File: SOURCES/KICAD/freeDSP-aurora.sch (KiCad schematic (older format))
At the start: 76 parts, among them IC101 IC_ADAU1452, IC102 IC_25AA1024, IC103 IC_TLE2426ID, IC104 IC_ADM811TARTZ, IC105 IC_LM1117MP-5.0, IC106 IC_NCP1117LPST33, IC107 IC_LM1117MP-5.0, IC108 IC_LM1117MPX-ADJ, Q101 Q_STD2805, X101 MicroMatch14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

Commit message: Updated BOM
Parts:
- C101: Manufacturer (none) -> Murata Electronics North America; manf_num (none) -> GRM21BR61E106MA73L; pn (none) -> GRM21BR61E106MA73L
- C102, C105, C109, C110, C113, C118, C121, C124, C128, C129, C130, C131, C133, C134, C135, C136: Manufacturer (none) -> KEMET; pn (none) -> C0805C104K5RACTU
- C103: Manufacturer (none) -> Yageo; pn (none) -> CC0805KRX7R9BB562
- C104, C111, C112, C114, C117, C119, C120, C122, C123, C125, C127, C132, C137: Manufacturer (none) -> Murata Electronics North America; pn (none) -> GRM21BR61E106MA73L
- C106: Manufacturer (none) -> KEMET; pn (none) -> C0805C151J5GACTU
- C107, C108: Manufacturer (none) -> KEMET; pn (none) -> C0805C220J5GACTU
- C115, C116, C126: Manufacturer (none) -> Wurth Electronics Inc.; pn (none) -> 860010474012
- FER101, FER102: Manufacturer (none) -> Murata Electronics North America; pn (none) -> BLM21AG601SN1D
- IC101: Manufacturer (none) -> Analog Devices Inc.; pn (none) -> ADAU1452WBCPZ
- IC102: Manufacturer (none) -> Microchip Technology; pn (none) -> 25AA1024T-I/SM
- IC103: Manufacturer (none) -> Texas Instruments; pn (none) -> TLE2426IDR
- IC104: Manufacturer (none) -> Analog Devices Inc.; pn (none) -> ADM811TARTZ-REEL
- IC105, IC107: Manufacturer (none) -> Texas Instruments; pn (none) -> LM1117MP-5.0/NOPB
- IC106: Manufacturer (none) -> ON Semiconductor; pn (none) -> NCP1117LPST33T3G
- IC108: Manufacturer (none) -> Texas Instruments; pn (none) -> LM1117MPX-ADJ/NOPB
- JP101: Manufacturer (none) -> Wurth Electronics Inc.; pn (none) -> 61300211121
- Q101: Manufacturer (none) -> STMicroelectronics; pn (none) -> STD2805T4
- R101, R102, R104, R105: Manufacturer (none) -> Yageo; pn (none) -> TC164-JR-0733RL
- R103, R114: Manufacturer (none) -> Yageo; pn (none) -> RC0805FR-071KL
- R106: Manufacturer (none) -> Yageo; pn (none) -> RC0805FR-074K32L
- R107, R112, R113: Manufacturer (none) -> Yageo; pn (none) -> RC0805FR-0710KL
- R108: Manufacturer (none) -> Yageo; pn (none) -> RC0805FR-07100RL
- R109: Manufacturer (none) -> Yageo; pn (none) -> RC0805FR-0733RL
- R110, R111: Manufacturer (none) -> Yageo; pn (none) -> RC0805FR-072KL
- R115: Manufacturer (none) -> Yageo; pn (none) -> RC0805FR-07100KL
- R116: Manufacturer (none) -> Stackpole Electronics Inc.; pn (none) -> RNCP0805FTD150R
- R117: Manufacturer (none) -> Yageo; pn (none) -> RC0805FR-07931RL
- X101: Manufacturer (none) -> TE Connectivity AMP Connectors; pn (none) -> 1-215079-4
- X102: Manufacturer (none) -> Sullins Connector Solutions; pn (none) -> PRPC008DAAN-RC
- X103: Manufacturer (none) -> Sullins Connector Solutions; pn (none) -> PRPC003SAAN-RC
- X104: Manufacturer (none) -> TE Connectivity AMP Connectors; pn (none) -> 1-215079-0
- X105: Manufacturer (none) -> Molex, LLC; pn (none) -> 0430450428
- Y101: Manufacturer (none) -> EPSON; pn (none) -> FA-238 24.5760MB-K3

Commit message: Improved ADC input stage
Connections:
- wire segments 363 -> 367
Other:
- moved on the sheet: C112, C113, C114, C115, C116, C137, R116

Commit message: Added extra LDO for ESP32
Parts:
- removed C112, C114, C137: CAP_10u0_25V_X5R_0805, rklib:C0805-X7R, symbol rk:CAP_10u0_25V_X5R_0805
- removed C113: CAP_100n_50V_X7R_0805, rklib:C0805-X7R, symbol rk:CAP_100n_50V_X7R_0805
- removed IC108: IC_LM1117MPX-ADJ, rklib:SOT223, symbol rk:IC_LM1117MPX-ADJ
- removed R116: RES_150R_1%_0.25W_Thin_0805, rklib:C0805-RES, symbol rk:RES_150R_1%_0.25W_Thin_0805
- removed R117: RES_931R_1%_0.125W_Thick_0805, rklib:C0805-RES, symbol rk:RES_931R_1%_0.125W_Thick_0805
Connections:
- net labels removed: +9VA
- wire segments 367 -> 347
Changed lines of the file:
@@
-$EndComp
-$Comp
-L freeDSP-aurora-rescue:GND #PWR011
-U 1 1 590AE9CB
-P 7100 12500
-F 0 "#PWR011" H 7100 12250 50  0001 C CNN
-F 1 "GND" H 7100 12350 39  0000 C CNN
-F 2 "" H 7100 12500 50  0000 C CNN
-F 3 "" H 7100 12500 50  0000 C CNN
-	1    7100 12500
-	1    0    0    -1
-$EndComp
-$Comp
-L freeDSP-aurora-rescue:GND #PWR012
-U 1 1 590AE9E1
-P 6900 12500
-F 0 "#PWR012" H 6900 12250 50  0001 C CNN
-F 1 "GND" H 6900 12350 39  0000 C CNN
-F 2 "" H 6900 12500 50  0000 C CNN
-F 3 "" H 6900 12500 50  0000 C CNN
-	1    6900 12500
-	1    0    0    -1
-$EndComp
-$Comp
-L freeDSP-aurora-rescue:GND #PWR013
-U 1 1 590AEA02
-P 5900 12500
-F 0 "#PWR013" H 5900 12250 50  0001 C CNN
-F 1 "GND" H 5900 12350 39  0000 C CNN
-F 2 "" H 5900 12500 50  0000 C CNN
-F 3 "" H 5900 12500 50  0000 C CNN
-	1    5900 12500
-	1    0    0    -1
-$EndComp
-$Comp
-L freeDSP-aurora-rescue:+12V #PWR014
-U 1 1 590AEA0B
-P 5900 12100
-F 0 "#PWR014" H 5900 11950 50  0001 C CNN
-F 1 "+12V" H 5900 12240 39  0000 C CNN
-F 2 "" H 5900 12100 50  0000 C CNN
-F 3 "" H 5900 12100 50  0000 C CNN
-	1    5900 12100
-	1    0    0    -1
 $EndComp
 $Comp
@@
 Text Label 5050 5550 2    39   ~ 0
 AUXADC5
-$Comp
-L freeDSP-aurora-rescue:GND #PWR059
-U 1 1 59F06A35
-P 6100 12850
-F 0 "#PWR059" H 6100 12600 50  0001 C CNN
-F 1 "GND" H 6100 12700 39  0000 C CNN
-F 2 "" H 6100 12850 50  0000 C CNN
-F 3 "" H 6100 12850 50  0000 C CNN
-	1    6100 12850
-	1    0    0    -1
-$EndComp
-$Comp
-L freeDSP-aurora-rescue:GND #PWR060
-U 1 1 59F06B0F
-P 6350 12850
-F 0 "#PWR060" H 6350 12600 50  0001 C CNN
-F 1 "GND" H 6350 12700 39  0000 C CNN
-F 2 "" H 6350 12850 50  0000 C CNN
-F 3 "" H 6350 12850 50  0000 C CNN
-	1    6350 12850
-	1    0    0    -1
-$EndComp
 Wire Wire Line
 	1450 10400 1500 10400
@@
 Connection ~ 2800 10300
 Connection ~ 3000 10300
-Wire Wire Line
-	6900 12150 6900 12200
-Wire Wire Line
-	7100 12100 7100 12150
-Connection ~ 6900 12150
-Connection ~ 5900 12150
-Connection ~ 7100 12150
-Wire Wire Line
-	5950 12150 5900 12150
 Wire Wire Line
 	6550 4000 6500 4000
@@
 Wire Wire Line
 	4800 5550 5050 5550
-Wire Wire Line
-	6350 12450 6350 12500
-Wire Wire Line
-	6100 12500 6350 12500
-Connection ~ 6350 12500
-Wire Wire Line
-	6750 12500 6700 12500
-Wire Wire Line
-	6100 12500 6100 12550
 $Sheet
 S 1200 2850 2250 1750
@@
 	1    0    0    -1
 $EndComp
-$Comp
-L freeDSP-aurora-rescue:+9VA #PWR072
-U 1 1 5B7A7F08
-P 7100 12100
-F 0 "#PWR072" H 7100 11975 50  0001 C CNN
-F 1 "+9VA" H 7100 12250 39  0000 C CNN
-F 2 "" H 7100 12100 50  0001 C CNN
-F 3 "" H 7100 12100 50  0001 C CNN
-	1    7100 12100
-	1    0    0    -1
-$EndComp
 Text Label 4050 6400 2    39   ~ 0
 xSDA
@@
 $EndComp
 Wire Wire Line
-	7350 12150 7350 12200
-Wire Wire Line
-	7600 12150 7600 12200
-Connection ~ 7350 12150
-Wire Wire Line
-	6750 12150 6900 12150
-Wire Wire Line
 	4600 10400 4600 10450
 Connection ~ 4350 10400
-Wire Wire Line
-	5900 12100 5900 12150
 $Comp
 L freeDSP-aurora-rescue:+12V #PWR076
@@
 	3000 10300 3000 10450
 Wire Wire Line
-	6900 12150 7100 12150
-Wire Wire Line
-	5900 12150 5900 12200
-Wire Wire Line
-	7100 12150 7100 12200
-Wire Wire Line
-	7100 12150 7350 12150
-Wire Wire Line
 	6500 5600 6500 6100
 Wire Wire Line
@@
 	6900 3600 6800 3600
 Wire Wire Line
-	6350 12500 6350 12550
-Wire Wire Line
-	6350 12500 6400 12500
-Wire Wire Line
 	11950 3200 11950 3250
 Wire Wire Line
@@
 Wire Wire Line
 	3250 10300 3250 10450
-Wire Wire Line
-	7350 12150 7600 12150
 Wire Wire Line
 	4350 10400 4600 10400
@@
 F 8 "BLM21AG601SN1D" H 0   0   50  0001 C CNN "pn"
 	1    5650 4400
-	0    1    1    0
-$EndComp
-$Comp
-L rk:CAP_100n_50V_X7R_0805 C113
-U 1 1 5C1D47A6
-P 6900 12350
-F 0 "C113" H 7100 12400 39  0000 R CNN
-F 1 "CAP_100n_50V_X7R_0805" H 6900 12200 39  0001 C CNN
-F 2 "rklib:C0805-X7R" H 6900 12150 39  0001 C CNN
-F 3 "" H 6950 12400 50  0001 C CNN
-F 4 "100n" H 7100 12450 39  0000 R CNN "Value1"
-F 5 "5% 50V X7R" H 6900 12100 39  0001 C CNN "Value2"
-F 6 "399-1170-1-ND" H 6900 12050 39  0001 C CNN "digikey"
-F 7 "KEMET" H 650 1850 50  0001 C CNN "Manufacturer"
-F 8 "C0805C104K5RACTU" H 650 1850 50  0001 C CNN "pn"
-	1    6900 12350
 	0    1    1    0
 $EndComp
@@
 $EndComp
 $Comp
-L rk:CAP_10u0_25V_X5R_0805 C112
-U 1 1 5C5046DC
-P 5900 12350
-F 0 "C112" H 6100 12400 39  0000 R CNN
-F 1 "CAP_10u0_25V_X5R_0805" H 5900 12200 39  0001 C CNN
-F 2 "rklib:C0805-X7R" H 5900 12150 39  0001 C CNN
-F 3 "" H 5950 12400 50  0001 C CNN
-F 4 "10u0" H 6100 12450 39  0000 R CNN "Value1"
-F 5 "20% 25V X5R" H 5900 12100 39  0001 C CNN "Value2"
-F 6 "490-10748-1-ND" H 5900 12050 39  0001 C CNN "digikey"
-F 7 "Murata Electronics North America" H 650 1850 50  0001 C CNN "Manufacturer"
-F 8 "GRM21BR61E106MA73L" H 650 1850 50  0001 C CNN "pn"
-	1    5900 12350
-	0    1    1    0
-$EndComp
-$Comp
-L rk:CAP_10u0_25V_X5R_0805 C114
-U 1 1 5C527B3F
-P 7100 12350
-F 0 "C114" H 7300 12400 39  0000 R CNN
-F 1 "CAP_10u0_25V_X5R_0805" H 7100 12200 39  0001 C CNN
-F 2 "rklib:C0805-X7R" H 7100 12150 39  0001 C CNN
-F 3 "" H 7150 12400 50  0001 C CNN
-F 4 "10u0" H 7300 12450 39  0000 R CNN "Value1"
-F 5 "20% 25V X5R" H 7100 12100 39  0001 C CNN "Value2"
-F 6 "490-10748-1-ND" H 7100 12050 39  0001 C CNN "digikey"
-F 7 "Murata Electronics North America" H 650 1850 50  0001 C CNN "Manufacturer"
-F 8 "GRM21BR61E106MA73L" H 650 1850 50  0001 C CNN "pn"
-	1    7100 12350
-	0    1    1    0
-$EndComp
-$Comp
 L rk:CAP_10u0_25V_X5R_0805 C111
 U 1 1 5C54CAEC
@@
 $EndComp
 $Comp
-L rk:IC_LM1117MPX-ADJ IC108
-U 1 1 5E2476C5
-P 6350 12200
-F 0 "IC108" H 6350 12493 39  0000 C CNN
-F 1 "IC_LM1117MPX-ADJ" H 6350 11850 39  0001 C CNN
-F 2 "rklib:SOT223" H 6350 11750 39  0001 C CIN
-F 3 "" H 6350 12200 50  0000 C CNN
-F 4 "LM1117MPX-ADJ" H 6350 12418 39  0000 C CNN "Value1"
-F 5 "LDO" H 6350 11650 39  0001 C CNN "Value2"
-F 6 "LM1117MPX-ADJ/NOPBCT-ND" H 6350 11550 39  0001 C CNN "digikey"
-F 7 "Texas Instruments" H 650 1850 50  0001 C CNN "Manufacturer"
-F 8 "LM1117MPX-ADJ/NOPB" H 650 1850 50  0001 C CNN "pn"
-	1    6350 12200
-	1    0    0    -1
-$EndComp
-$Comp
 L rk:IC_NCP1117LPST33 IC106
 U 1 1 5E24805E
@@
 Wire Wire Line
 	1950 10250 1950 10300
-Wire Wire Line
-	6750 12250 6750 12500
 Connection ~ 1950 10300
 Wire Wire Line
@@
 	4700 7800 5050 7800
 Connection ~ 5050 7800
-$Comp
-L rk:CAP_10u0_25V_X5R_0805 C137
-U 1 1 5BF3DC1A
-P 6100 12700
-F 0 "C137" H 6300 12750 39  0000 R CNN
-F 1 "CAP_10u0_25V_X5R_0805" H 6100 12550 39  0001 C CNN
-F 2 "rklib:C0805-X7R" H 6100 12500 39  0001 C CNN
-F 3 "" H 6150 12750 50  0001 C CNN
-F 4 "10u0" H 6300 12800 39  0000 R CNN "Value1"
-F 5 "20% 25V X5R" H 6100 12450 39  0001 C CNN "Value2"
-F 6 "490-10748-1-ND" H 6100 12400 39  0001 C CNN "digikey"
-F 7 "Murata Electronics North America" H 650 1850 50  0001 C CNN "Manufacturer"
-F 8 "GRM21BR61E106MA73L" H 650 1850 50  0001 C CNN "pn"
-	1    6100 12700
-	0    1    1    0
-$EndComp
-$Comp
-L rk:RES_931R_1%_0.125W_Thick_0805 R117
-U 1 1 5BF62D38
-P 6350 12700
-F 0 "R117" H 6350 12700 39  0000 C CNN
-F 1 "RES_931R_1%_0.125W_Thick_0805" H 6350 12525 39  0001 C CNN
-F 2 "rklib:C0805-RES" H 6350 12475 39  0001 C CNN
-F 3 "" H 6350 12700 50  0000 C CNN
-F 4 "931R" H 6350 12625 39  0000 C CNN "Value1"
-F 5 "1% 0.125W Thick" H 6350 12575 39  0001 C CNN "Value2"
-F 6 "311-931CRCT-ND" H 6350 12400 39  0001 C CNN "digikey"
-F 7 "Yageo" H 650 1850 50  0001 C CNN "Manufacturer"
-F 8 "RC0805FR-07931RL" H 650 1850 50  0001 C CNN "pn"
-	1    6350 12700
-	0    -1   1    0
-$EndComp
-$Comp
-L rk:RES_150R_1%_0.25W_Thin_0805 R116
-U 1 1 5BFABE4F
-P 6550 12500
-F 0 "R116" H 6550 12500 39  0000 C CNN
-F 1 "RES_150R_1%_0.25W_Thin_0805" H 6550 12325 39  0001 C CNN
-F 2 "rklib:C0805-RES" H 6550 12275 39  0001 C CNN
-F 3 "" H 6550 12500 50  0000 C CNN
-F 4 "150R" H 6550 12575 39  0000 C CNN "Value1"
-F 5 "1% 0.25W Thin" H 6550 12375 39  0001 C CNN "Value2"
-F 6 "RNCP0805FTD150RCT-ND" H 6550 12200 39  0001 C CNN "digikey"
-F 7 "Stackpole Electronics Inc." H 650 1850 50  0001 C CNN "Manufacturer"
-F 8 "RNCP0805FTD150R" H 650 1850 50  0001 C CNN "pn"
-	1    6550 12500
-	-1   0    0    1
-$EndComp
-Wire Wire Line
-	6750 12250 6750 12150
-Connection ~ 6750 12250
-Connection ~ 6750 12150
 Wire Wire Line
 	8300 7450 8300 7350

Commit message: Improved LDO heatsinking
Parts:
- removed X103: HDR_01x03, rklib:HDR_01x03, symbol freeDSP-aurora-rescue:CONN_01X03
- added X103: Conn_01x03, rklib:Molex_PicoBlade_530470310, symbol freeDSP-aurora-rescue:Conn_01x03
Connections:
- net +3V3: now also X103.1 (Pin_1)
- net AUXADC5: now also X103.2 (Pin_2)
- net GND: now also X103.3 (Pin_3)
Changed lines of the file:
@@
 xTDMIN
-$Comp
-L freeDSP-aurora-rescue:CONN_01X03 X103
-U 1 1 59EF7C06
-P 4600 5550
-F 0 "X103" H 4600 5750 39  0000 C CNN
-F 1 "HDR_01x03" V 4700 5550 39  0000 C CNN
-F 2 "rklib:HDR_01x03" H 4600 5550 50  0001 C CNN
-F 3 "" H 4600 5550 50  0000 C CNN
-F 4 "HDR_01x03" H 0   0   50  0001 C CNN "Value1"
-F 5 "-" H 0   0   50  0001 C CNN "Value2"
-F 6 "???" H 0   0   50  0001 C CNN "digikey"
-F 7 "Sullins Connector Solutions" H 0   0   50  0001 C CNN "Manufacturer"
-F 8 "PRPC003SAAN-RC" H 0   0   50  0001 C CNN "pn"
-	1    4600 5550
-	-1   0    0    -1
-$EndComp
 $Comp
 L freeDSP-aurora-rescue:GND #PWR057
@@
 	5100 10400 5100 10450
 Connection ~ 4850 10400
+$Comp
+L freeDSP-aurora-rescue:Conn_01x03 X?
+U 1 1 5CBB0535
+P 4600 5550
+AR Path="/5B77113C/5CBB0535" Ref="X?"  Part="1"
+AR Path="/5CBB0535" Ref="X103"  Part="1"
+F 0 "X103" H 4600 5750 39  0000 C CNN
+F 1 "Conn_01x03" H 4600 5350 39  0001 C CNN
+F 2 "rklib:Molex_PicoBlade_530470310" H 4600 5550 50  0001 C CNN
+F 3 "" H 4600 5550 50  0001 C CNN
+F 4 "PB-01x03" H -3500 1550 50  0001 C CNN "Value1"
+F 5 "-" H -3500 1550 50  0001 C CNN "Value2"
+F 6 "???" H -3500 1550 50  0001 C CNN "digikey"
+F 7 "Molex, LLC" H -3500 1550 50  0001 C CNN "Manufacturer"
+F 8 "0530470310" H -3500 1550 50  0001 C CNN "pn"
+	1    4600 5550
+	-1   0    0    -1
+$EndComp
 $EndSCHEMATC

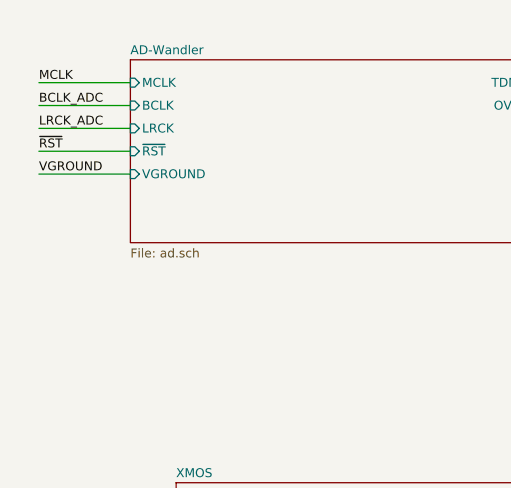
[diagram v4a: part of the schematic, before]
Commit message: I2C control of ADC
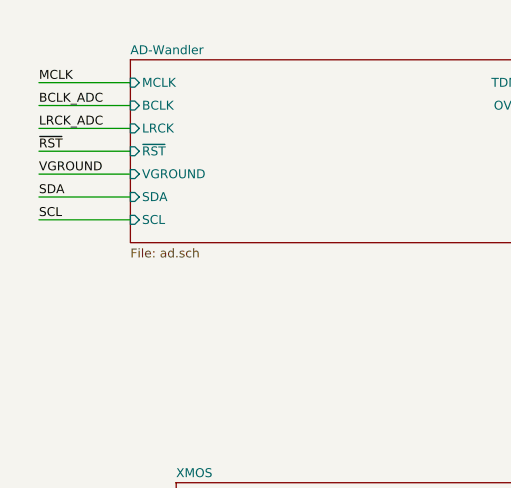
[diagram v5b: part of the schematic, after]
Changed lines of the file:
@@
 F7 "~RST" I L 1000 1400 39
 F8 "VGROUND" I L 1000 1500 39
+F9 "SDA" I L 1000 1600 39
+F10 "SCL" I L 1000 1700 39
 $EndSheet
 $Sheet
@@
 	-1   0    0    -1
 $EndComp
+Text Label 600  1600 0    39   ~ 0
+SDA
+Wire Wire Line
+	1000 1600 600  1600
+Text Label 600  1700 0    39   ~ 0
+SCL
+Wire Wire Line
+	1000 1700 600  1700
 $EndSCHEMATC

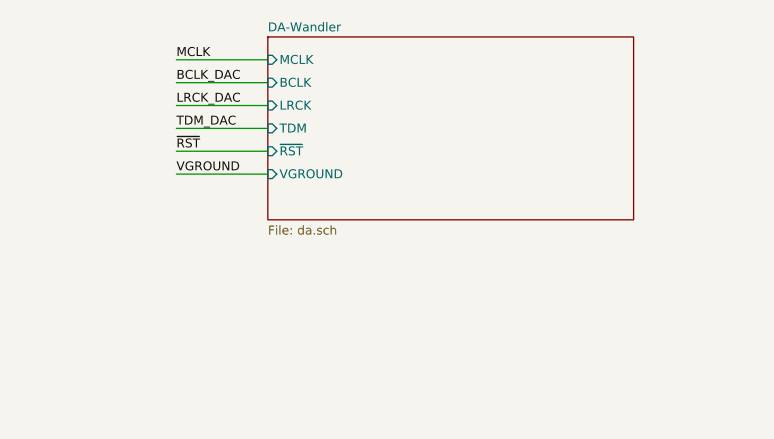
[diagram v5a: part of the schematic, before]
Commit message: I2C control of DAC
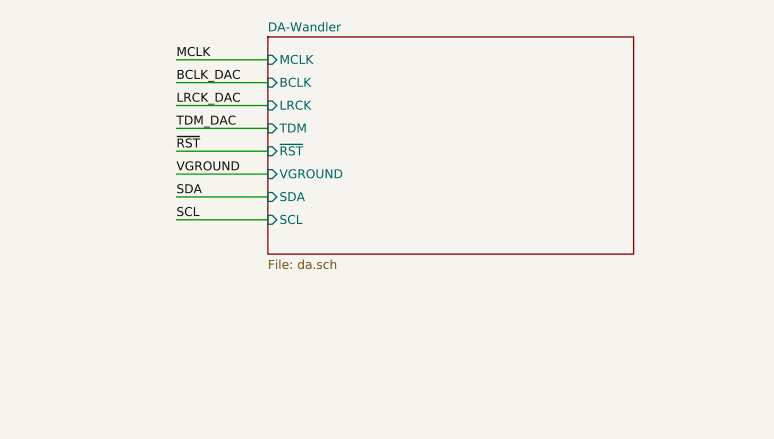
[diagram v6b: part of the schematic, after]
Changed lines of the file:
@@
 $EndSheet
 $Sheet
-S 13800 900  1600 800
+S 13800 900  1600 950
 U 5904EED5
 F0 "DA-Wandler" 39
@@
 F6 "TDM" I L 13800 1300 39
 F7 "VGROUND" I L 13800 1500 39
+F8 "SDA" I L 13800 1600 39
+F9 "SCL" I L 13800 1700 39
 $EndSheet
 $Comp
@@
 Wire Wire Line
 	1000 1700 600  1700
+Text Label 13400 1600 0    39   ~ 0
+SDA
+Wire Wire Line
+	13800 1600 13400 1600
+Text Label 13400 1700 0    39   ~ 0
+SCL
+Wire Wire Line
+	13800 1700 13400 1700
 $EndSCHEMATC

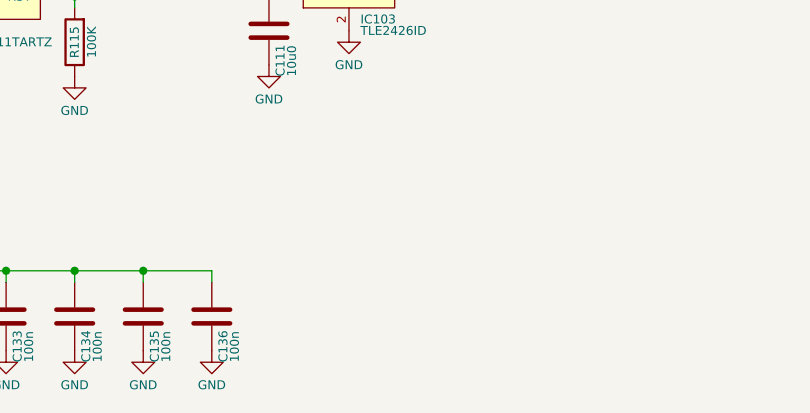
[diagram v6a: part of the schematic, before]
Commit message: Added connector for power LED
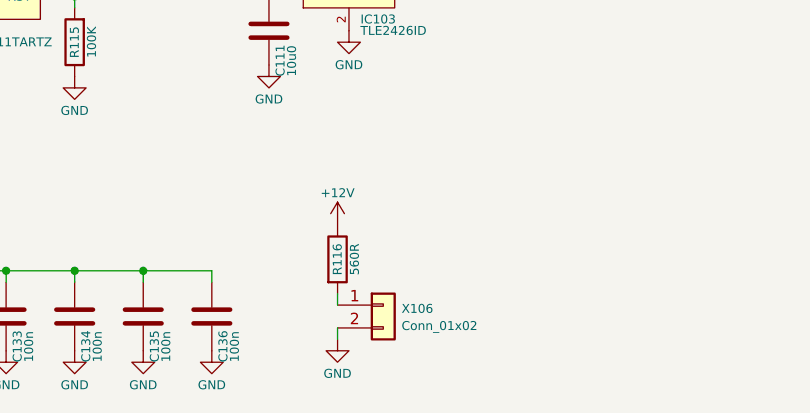
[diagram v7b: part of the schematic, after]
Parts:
- added R116: 560R, rklib:C0805-RES, symbol freeDSP-aurora-rescue:R
- added X106: Conn_01x02, rklib:HDR_01x02, symbol Connector_Generic:Conn_01x02
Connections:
- net +12V: now also R116.1
- net GND: now also X106.2 (Pin_2)
- new net: R116.2, X106.1 (Pin_1)
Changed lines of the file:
@@
 Wire Wire Line
 	13800 1700 13400 1700
+$Comp
+L freeDSP-aurora-rescue:R R116
+U 1 1 5CA37EA5
+P 11050 10500
+F 0 "R116" V 11050 10500 39  0000 C CNN
+F 1 "560R" V 11125 10500 39  0000 C CNN
+F 2 "rklib:C0805-RES" V 10980 10500 50  0001 C CNN
+F 3 "" H 11050 10500 50  0000 C CNN
+F 4 "560R" H 3850 4050 50  0001 C CNN "Value1"
+F 5 "1% 0.125W Thick" H 3850 4050 50  0001 C CNN "Value2"
+F 6 "???" H 3850 4050 50  0001 C CNN "digikey"
+F 7 "" H 3850 4050 50  0001 C CNN "Manufacturer"
+F 8 "" H 3850 4050 50  0001 C CNN "pn"
+	1    11050 10500
+	1    0    0    -1
+$EndComp
+$Comp
+L freeDSP-aurora-rescue:GND #PWR0135
+U 1 1 5CA5AE95
+P 11050 10850
+F 0 "#PWR0135" H 11050 10600 50  0001 C CNN
+F 1 "GND" H 11050 10700 39  0000 C CNN
+F 2 "" H 11050 10850 50  0000 C CNN
+F 3 "" H 11050 10850 50  0000 C CNN
+	1    11050 10850
+	1    0    0    -1
+$EndComp
+$Comp
+L Connector_Generic:Conn_01x02 X106
+U 1 1 5CAC0491
+P 11250 10700
+F 0 "X106" H 11330 10684 39  0000 L CNN
+F 1 "Conn_01x02" H 11330 10609 39  0000 L CNN
+F 2 "rklib:HDR_01x02" H 11250 10700 50  0001 C CNN
+F 3 "~" H 11250 10700 50  0001 C CNN
+	1    11250 10700
+	1    0    0    -1
+$EndComp
+Wire Wire Line
+	11050 10700 11050 10650
+Wire Wire Line
+	11050 10850 11050 10800
+$Comp
+L freeDSP-aurora-rescue:+12V #PWR?
+U 1 1 5CB0EFA6
+P 11050 10350
+F 0 "#PWR?" H 11050 10200 50  0001 C CNN
+F 1 "+12V" H 11050 10490 39  0000 C CNN
+F 2 "" H 11050 10350 50  0000 C CNN
+F 3 "" H 11050 10350 50  0000 C CNN
+	1    11050 10350
+	1    0    0    -1
+$EndComp
 $EndSCHEMATC
